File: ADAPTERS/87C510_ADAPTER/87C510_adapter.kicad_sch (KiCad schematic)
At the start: 12 parts, among them J1 ROM, U1 TMS87C510, U2 74LVC1G04

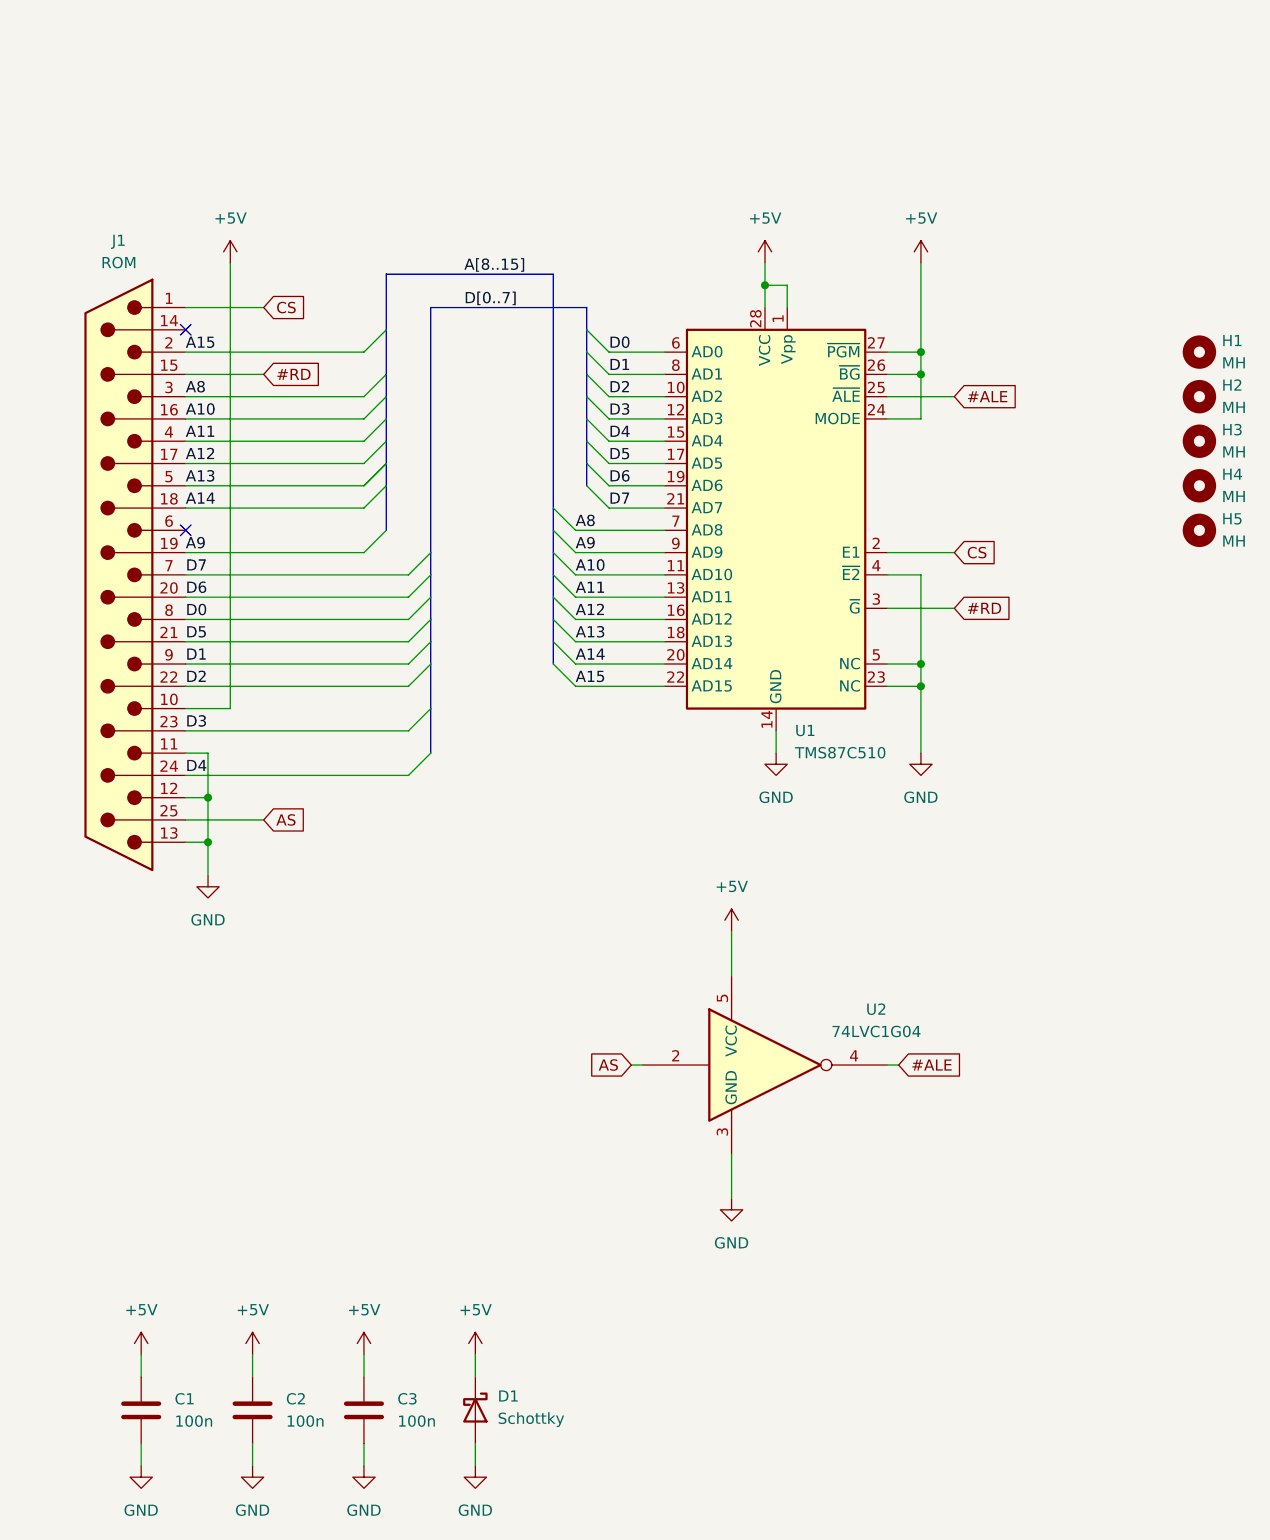
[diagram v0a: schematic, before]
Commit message: Fixed 87C510 project, as inverter gate for ALE signal was not required
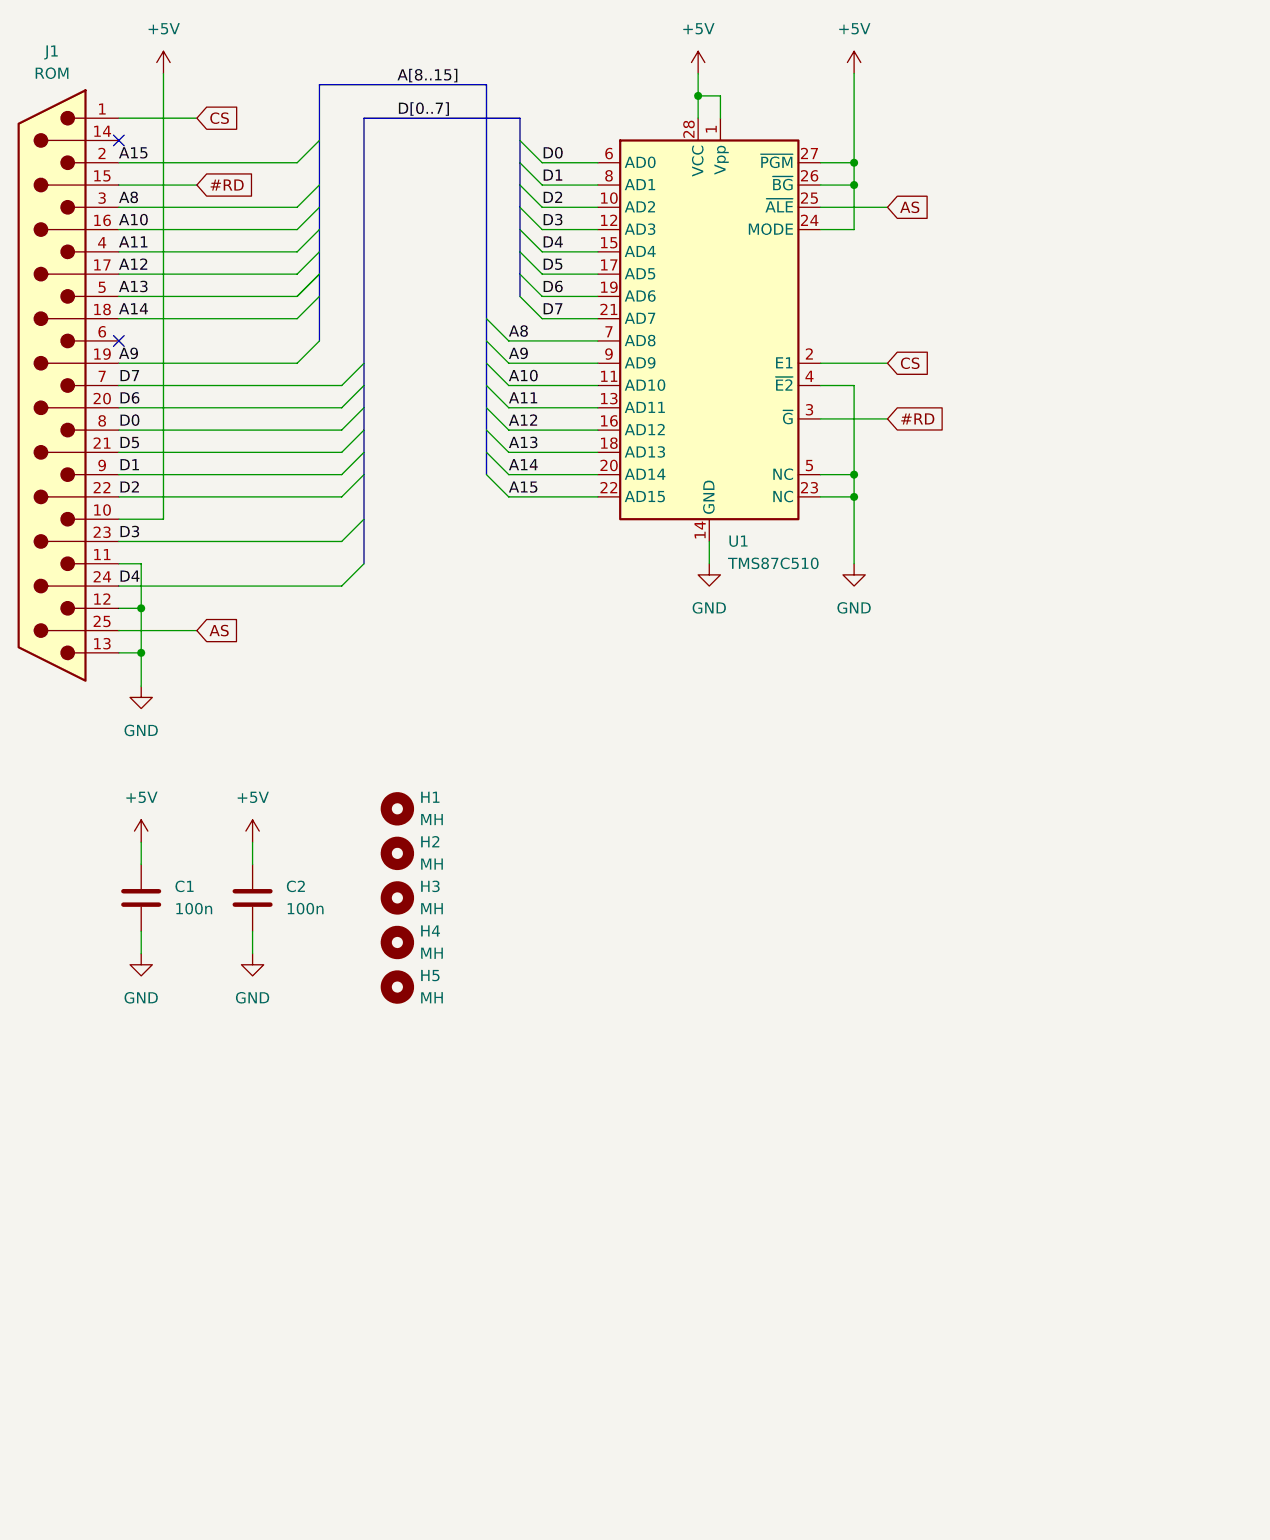
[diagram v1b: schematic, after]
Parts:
- removed C3: 100n, Capacitor_SMD:C_1206_3216Metric_Pad1.33x1.80mm_HandSolder, symbol Device:C
- removed D1: Schottky, Diode_SMD:D_SMB_Handsoldering, symbol Device:D_Schottky
- removed U2: 74LVC1G04, Package_TO_SOT_SMD:SOT-23-5_HandSoldering, symbol 74xGxx:74LVC1G04
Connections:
- net #ALE is gone; now on net AS: U1.25 (~{ALE})
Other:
- moved on the sheet: C1, C2, H1, H2, H3, H4, H5, J1, U1
